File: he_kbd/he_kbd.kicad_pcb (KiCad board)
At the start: 2 copper layers, 162.2 x 126.5 mm, 175 parts

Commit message: more progress
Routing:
- net NEOPIXEL_POWER: track 914.5 -> 915.7 mm
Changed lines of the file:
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@@
 	)
 	(segment
-		(start 138.240183 50.844942)
+		(start 128.040183 50.844942)
 		(end 121.640183 50.844942)
 		(width 0.7)
@@
 	)
 	(segment
+		(start 138.240183 50.844942)
+		(end 128.040183 50.844942)
+		(width 0.7)
+		(layer "B.Cu")
+		(net 23)
+	)
+	(segment
 		(start 152.460183 85.544942)
 		(end 152.660183 85.344942)
@@
 	)
 	(segment
+		(start 127.990183 50.894942)
+		(end 128.040183 50.844942)
+		(width 0.7)
+		(layer "B.Cu")
+		(net 23)
+	)
+	(segment
 		(start 60.590183 129.094942)
 		(end 59.090183 129.094942)
@@
 		(width 0.7)
 		(layer "B.Cu")
+		(net 23)
+	)
+	(segment
+		(start 127.990183 52.044942)
+		(end 127.990183 50.894942)
+		(width 0.7)
+		(layer "B.Cu")

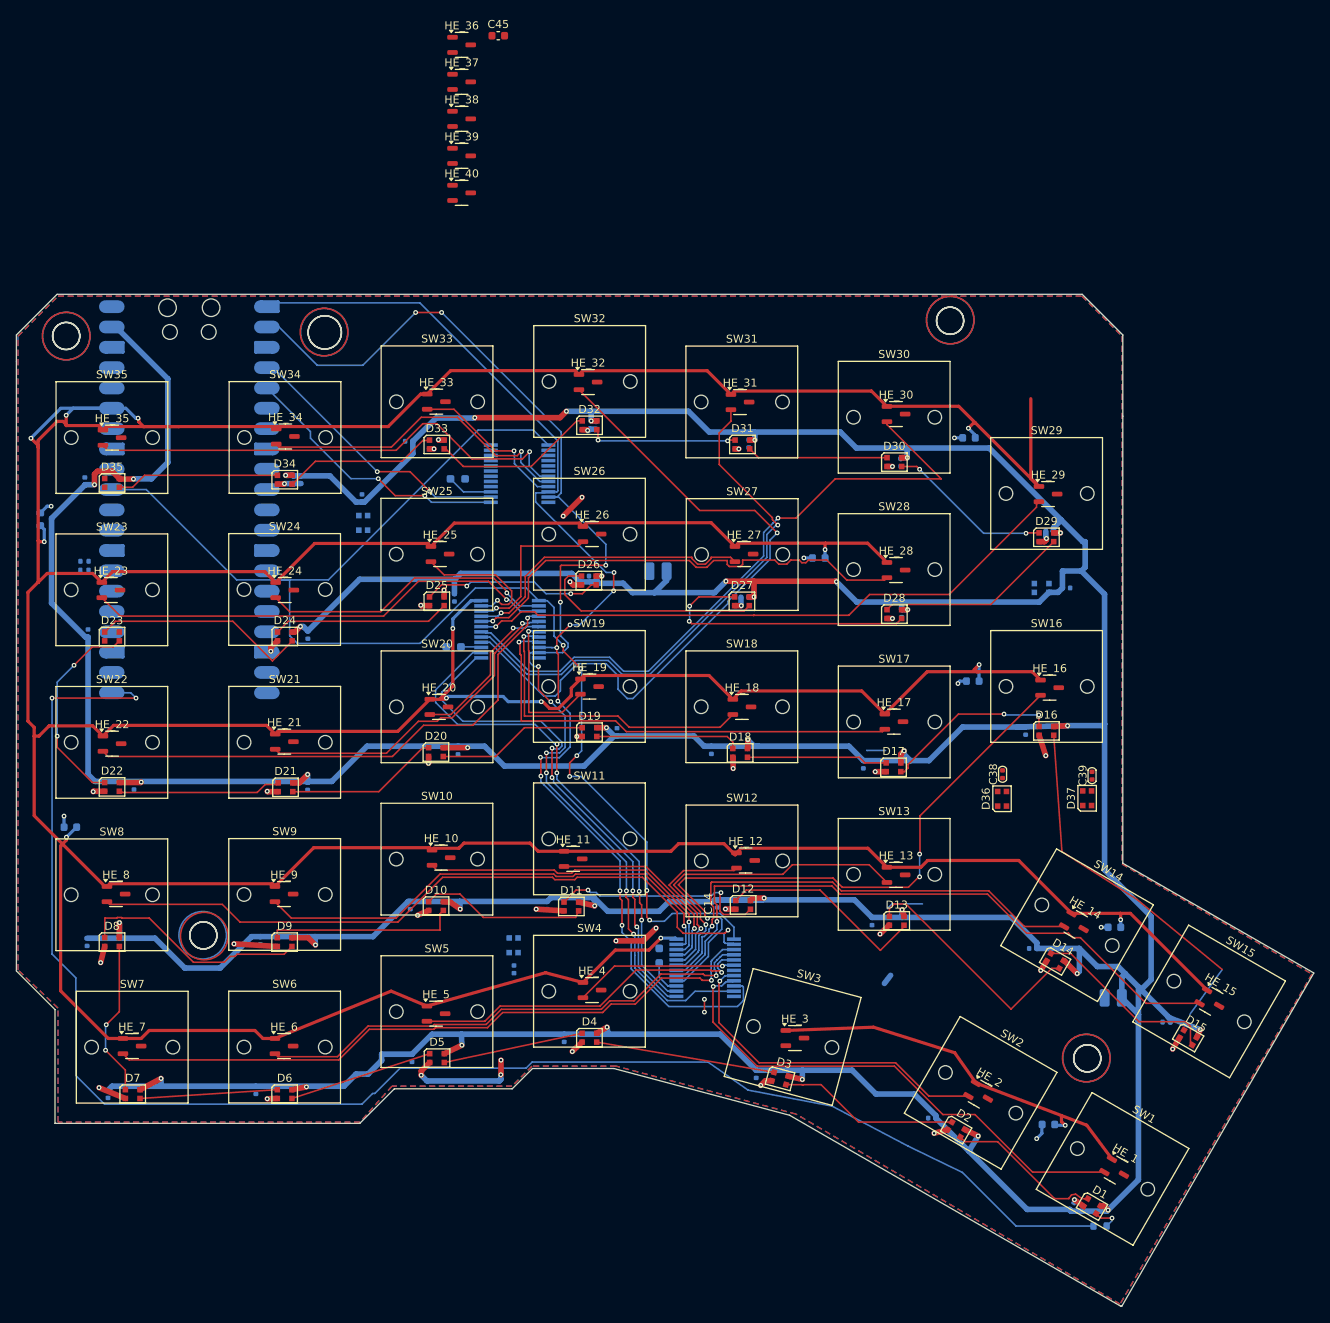
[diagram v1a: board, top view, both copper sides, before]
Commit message: realised have to change capacitor footprint entirely
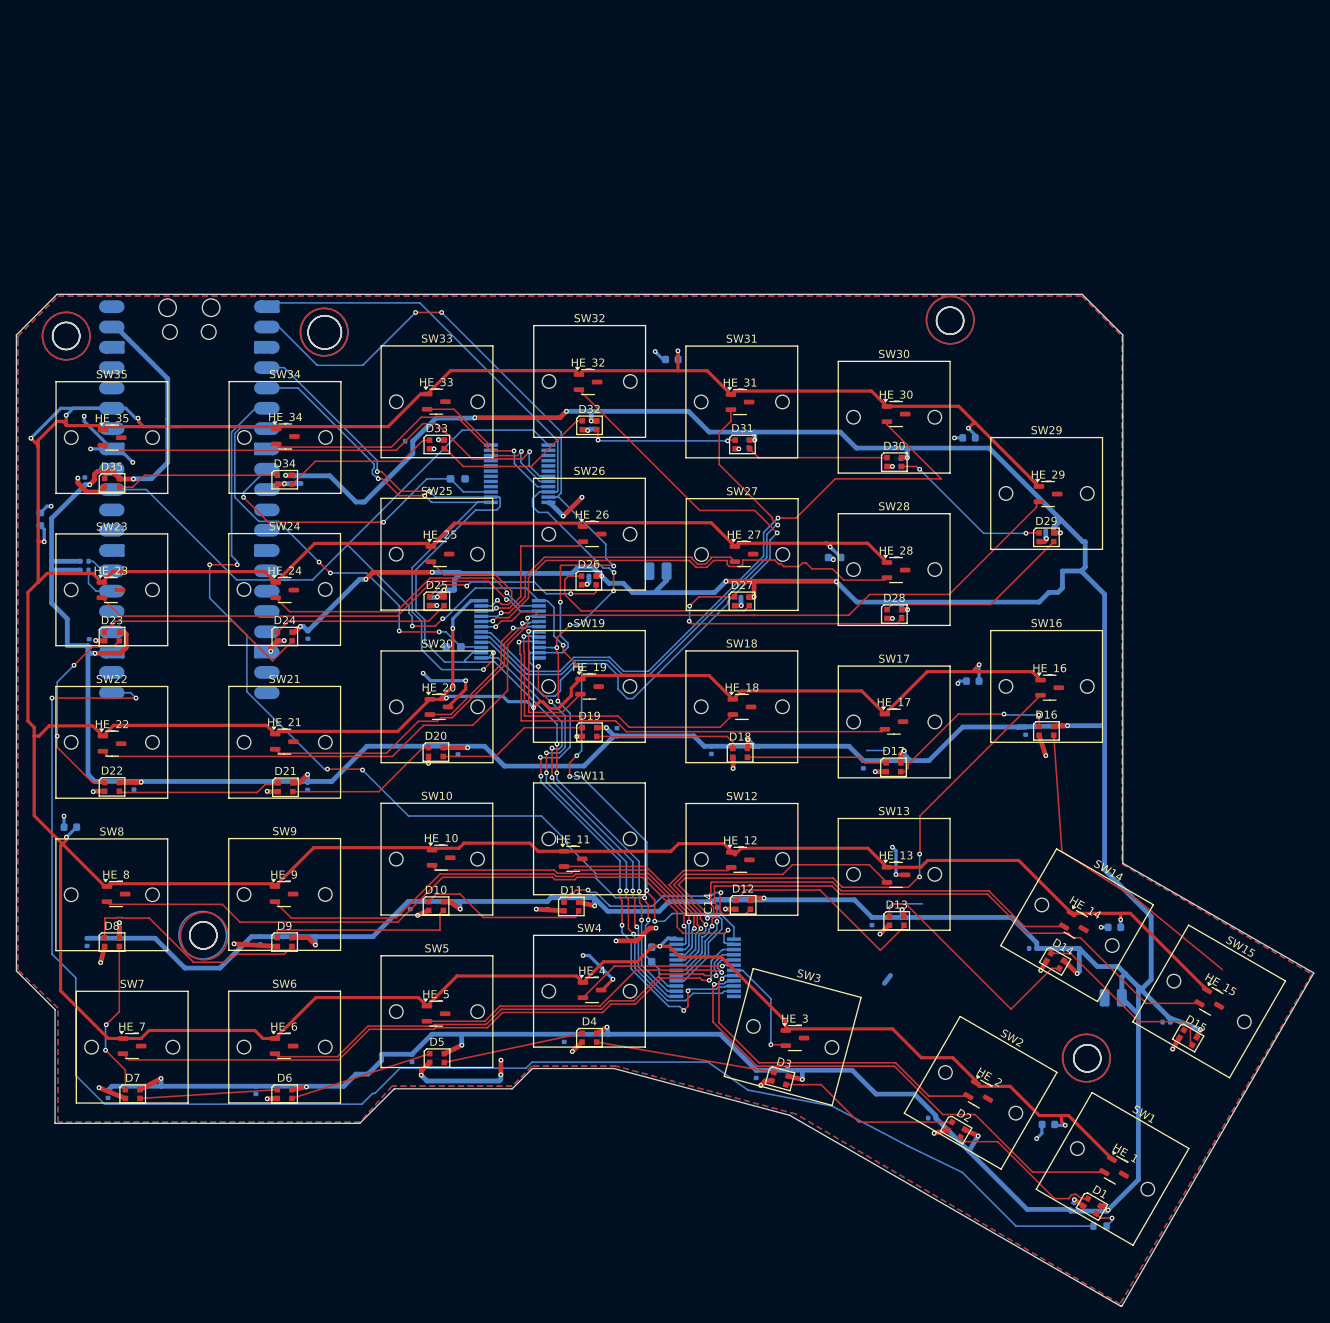
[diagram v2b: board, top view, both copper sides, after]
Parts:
- removed C38, C39, C40, C41, C42: 100n, PCM_Capacitor_SMD_AKL:C_0402_1005Metric
- removed D36, D37, D38, D39, D40: WS2812B-2020, LED_SMD:LED_WS2812B-2020_PLCC4_2.0x2.0mm
- removed HE_36, HE_37, HE_38, HE_39, HE_40: ~, Package_TO_SOT_SMD:SOT-23-3
- C45: moved to B.Cu
- moved C45 45.9 mm to (98.6, 39.8), turned to 180 degrees
- moved C27 3.02 mm to (68.4, 70.0)
- moved C47 1.98 mm to (118.9, 64.5)
- moved C25 1.24 mm to (25.7, 75.2)
- moved R9 0.95 mm to (96.1, 114.1)
- moved HE_12 0.66 mm to (107.1, 102.3)
- moved SW12 0.19 mm to (100.3, 95.2)
- turned R6 to 0 degrees
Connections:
- AM2 pad 2: /hesig40 -> unconnected-(AM2-I7-Pad2)
- AM2 pad 3: /hesig39 -> unconnected-(AM2-I6-Pad3)
- AM2 pad 4: /hesig38 -> unconnected-(AM2-I5-Pad4)
- AM2 pad 5: /hesig37 -> unconnected-(AM2-I4-Pad5)
- AM2 pad 6: /hesig36 -> unconnected-(AM2-I3-Pad6)
- D35 pad 1: Net-(D35-DOUT) -> unconnected-(D35-DOUT-Pad1)
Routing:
- net /MTP_EN_0: track 4.38 -> 118.3 mm, vias 0 -> 6
- net /MTP_EN_1: track 2.57 -> 52.7 mm, vias 0 -> 4
- net /ANALOGUE_GND: track 9.37 -> 44.2 mm, vias 7 -> 17
- net /MTP_EN_2: track 5.72 -> 39.8 mm, vias 0 -> 2
- net /MTP_BIN_3: track 99.3 -> 128.1 mm, vias 6 -> 8
- net /MTP_BIN_2: track 98.9 -> 124.8 mm
- net NEOPIXEL_POWER: track 915.7 -> 938.2 mm, vias 39 -> 43
- net /ANALOGUE_VIN: track 825.6 -> 845.5 mm, vias 14 -> 15
- net /hesig3: track 0.00 -> 13.8 mm, vias 0 -> 1
- net /AN_SIG: track 172.4 -> 162.0 mm, vias 6 -> 8
- net GND: track 82.0 -> 90.2 mm, vias 41 -> 42
- net Net-(D15-DOUT): track 46.4 -> 39.5 mm
- net I2C0_SDA: track 0.00 -> 4.98 mm
- net I2C0_SCL: track 0.00 -> 3.40 mm
- net /MTP_BIN_1: track 153.4 -> 155.0 mm
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
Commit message: i will have to change the led footprint as well lets go
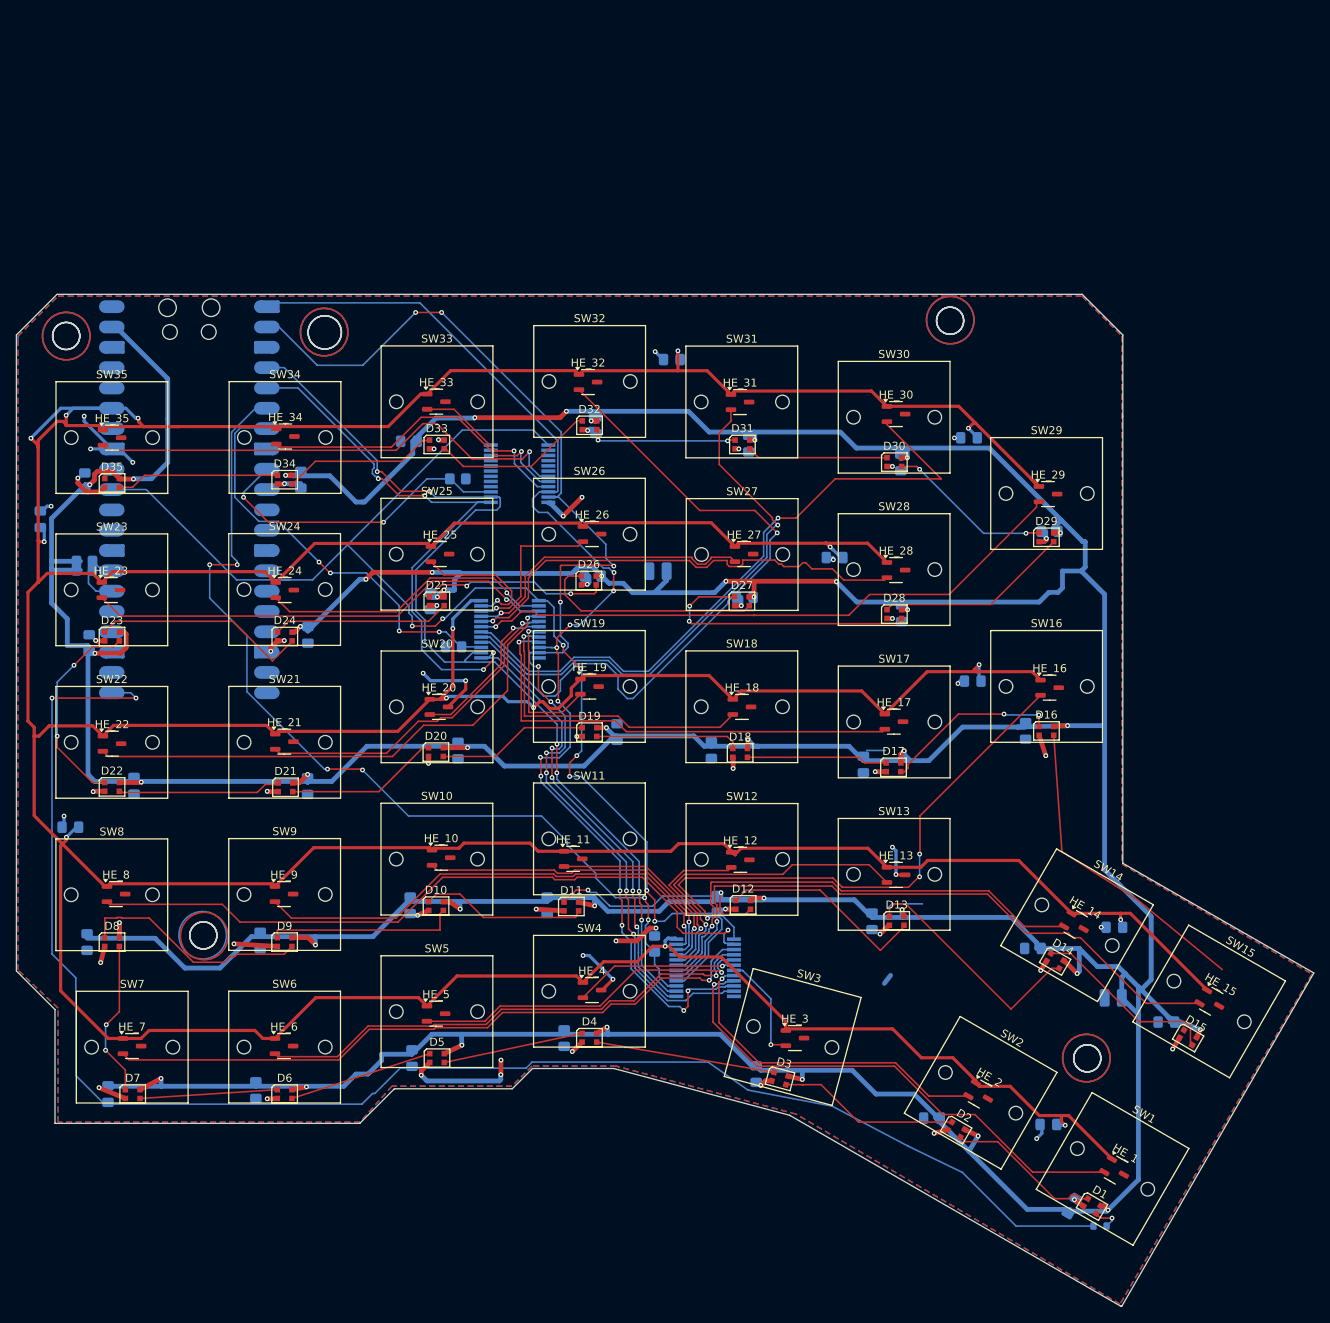
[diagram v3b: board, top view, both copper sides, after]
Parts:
- C10, C11, C12, C13, C14, C15, C16, C17, C18, C19, C20, C21, C22, C23, C24, C25, C26, C27, C28, C29, C3, C30, C31, C32, C33, C34, C35, C36, C37, C4, C5, C6, C7, C8, C9: footprint PCM_Capacitor_SMD_AKL:C_0402_1005Metric -> PCM_Capacitor_SMD_AKL:C_0805_2012Metric_Pad1.18x1.45mm_HandSolder
- C43, C44, C45, C46, C47, C48, C49, C50: footprint Inductor_SMD:L_0603_1608Metric -> PCM_Capacitor_SMD_AKL:C_0805_2012Metric_Pad1.18x1.45mm_HandSolder
- R5, R6: footprint Resistor_SMD:R_0402_1005Metric -> Resistor_SMD:R_0805_2012Metric_Pad1.20x1.40mm_HandSolder
- R7, R8, R9: footprint Resistor_SMD:R_0603_1608Metric_Pad0.98x0.95mm_HandSolder -> Resistor_SMD:R_0805_2012Metric_Pad1.20x1.40mm_HandSolder
- moved R9 1.36 mm to (96.4, 112.8)

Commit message: regaining progress, slowly remapping the broken connectiosn
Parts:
- D1, D10, D11, D12, D13, D14, D15, D16, D17, D18, D19, D2, D20, D21, D22, D23, D24, D25, D26, D27, D28, D29, D3, D30, D31, D32, D33, D34, D35, D4, D5, D6, D7, D8, D9: value WS2812B-2020 -> WS2812B; footprint LED_SMD:LED_WS2812B-2020_PLCC4_2.0x2.0mm -> LED_SMD:LED_WS2812B_PLCC4_5.0x5.0mm_P3.2mm
- moved C13 5.42 mm to (88.3, 106.9)
- moved C19 3.96 mm to (126.4, 90.9)
- moved C20 3.80 mm to (107.2, 89.3)
- moved C8 3.65 mm to (50.2, 131.7)
- moved C17 3.60 mm to (162.8, 125.3), turned to -90 degrees
- moved C4 3.56 mm to (133.9, 136.8), turned to -120 degrees
- moved C12 3.41 mm to (69.3, 108.4)
- moved C21 3.28 mm to (88.4, 86.6), turned to -90 degrees
- moved HE_11 3.18 mm to (88.2, 99.7)
- moved C9 3.15 mm to (31.2, 132.0)
- moved C7 3.00 mm to (69.1, 127.2)
- moved C11 2.99 mm to (50.1, 112.6)
- moved D11 2.99 mm to (88.3, 106.3)
- moved C10 2.97 mm to (28.4, 112.7)
- moved C16 2.89 mm to (146.1, 115.0), turned to -90 degrees
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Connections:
- D1 pad 1: Net-(D1-DOUT) -> NEOPIXEL_POWER
- D1 pad 2: GND -> Net-(D1-DOUT)
- D1 pad 3: Net-(D1-DIN) -> GND
- D1 pad 4: NEOPIXEL_POWER -> Net-(D1-DIN)
- D10 pad 1: Net-(D10-DOUT) -> NEOPIXEL_POWER
- D10 pad 2: GND -> Net-(D10-DOUT)
- D10 pad 3: Net-(D10-DIN) -> GND
- D10 pad 4: NEOPIXEL_POWER -> Net-(D10-DIN)
- D11 pad 1: Net-(D11-DOUT) -> NEOPIXEL_POWER
- D11 pad 2: GND -> Net-(D11-DOUT)
- D11 pad 3: Net-(D10-DOUT) -> GND
- D11 pad 4: NEOPIXEL_POWER -> Net-(D10-DOUT)
- D12 pad 1: Net-(D12-DOUT) -> NEOPIXEL_POWER
- D12 pad 2: GND -> Net-(D12-DOUT)
- D12 pad 3: Net-(D11-DOUT) -> GND
- D12 pad 4: NEOPIXEL_POWER -> Net-(D11-DOUT)
- D13 pad 1: Net-(D13-DOUT) -> NEOPIXEL_POWER
- D13 pad 2: GND -> Net-(D13-DOUT)
- D13 pad 3: Net-(D12-DOUT) -> GND
- D13 pad 4: NEOPIXEL_POWER -> Net-(D12-DOUT)
- D14 pad 1: Net-(D14-DOUT) -> NEOPIXEL_POWER
- D14 pad 2: GND -> Net-(D14-DOUT)
- D14 pad 3: Net-(D13-DOUT) -> GND
- D14 pad 4: NEOPIXEL_POWER -> Net-(D13-DOUT)
- D15 pad 1: Net-(D15-DOUT) -> NEOPIXEL_POWER
- D15 pad 2: GND -> Net-(D15-DOUT)
- D15 pad 3: Net-(D14-DOUT) -> GND
- D15 pad 4: NEOPIXEL_POWER -> Net-(D14-DOUT)
- D16 pad 1: Net-(D16-DOUT) -> NEOPIXEL_POWER
- D16 pad 2: GND -> Net-(D16-DOUT)
- D16 pad 3: Net-(D15-DOUT) -> GND
- D16 pad 4: NEOPIXEL_POWER -> Net-(D15-DOUT)
- D17 pad 1: Net-(D17-DOUT) -> NEOPIXEL_POWER
- D17 pad 2: GND -> Net-(D17-DOUT)
- D17 pad 3: Net-(D16-DOUT) -> GND
- D17 pad 4: NEOPIXEL_POWER -> Net-(D16-DOUT)
- D18 pad 1: Net-(D18-DOUT) -> NEOPIXEL_POWER
- D18 pad 2: GND -> Net-(D18-DOUT)
- D18 pad 3: Net-(D17-DOUT) -> GND
- D18 pad 4: NEOPIXEL_POWER -> Net-(D17-DOUT)
- D19 pad 1: Net-(D19-DOUT) -> NEOPIXEL_POWER
- D19 pad 2: GND -> Net-(D19-DOUT)
- D19 pad 3: Net-(D18-DOUT) -> GND
- D19 pad 4: NEOPIXEL_POWER -> Net-(D18-DOUT)
- D2 pad 1: Net-(D2-DOUT) -> NEOPIXEL_POWER
- D2 pad 2: GND -> Net-(D2-DOUT)
- D2 pad 3: Net-(D1-DOUT) -> GND
- D2 pad 4: NEOPIXEL_POWER -> Net-(D1-DOUT)
- D20 pad 1: Net-(D20-DOUT) -> NEOPIXEL_POWER
- D20 pad 2: GND -> Net-(D20-DOUT)
- D20 pad 3: Net-(D19-DOUT) -> GND
- D20 pad 4: NEOPIXEL_POWER -> Net-(D19-DOUT)
- D21 pad 1: Net-(D21-DOUT) -> NEOPIXEL_POWER
- D21 pad 2: GND -> Net-(D21-DOUT)
- D21 pad 3: Net-(D20-DOUT) -> GND
- D21 pad 4: NEOPIXEL_POWER -> Net-(D20-DOUT)
- D22 pad 1: Net-(D22-DOUT) -> NEOPIXEL_POWER
- D22 pad 2: GND -> Net-(D22-DOUT)
- D22 pad 3: Net-(D21-DOUT) -> GND
- D22 pad 4: NEOPIXEL_POWER -> Net-(D21-DOUT)
- D23 pad 1: Net-(D23-DOUT) -> NEOPIXEL_POWER
- D23 pad 2: GND -> Net-(D23-DOUT)
- D23 pad 3: Net-(D22-DOUT) -> GND
- D23 pad 4: NEOPIXEL_POWER -> Net-(D22-DOUT)
- D24 pad 1: Net-(D24-DOUT) -> NEOPIXEL_POWER
- D24 pad 2: GND -> Net-(D24-DOUT)
- D24 pad 3: Net-(D23-DOUT) -> GND
- D24 pad 4: NEOPIXEL_POWER -> Net-(D23-DOUT)
- D25 pad 1: Net-(D25-DOUT) -> NEOPIXEL_POWER
- D25 pad 2: GND -> Net-(D25-DOUT)
- D25 pad 3: Net-(D24-DOUT) -> GND
- D25 pad 4: NEOPIXEL_POWER -> Net-(D24-DOUT)
- D26 pad 1: Net-(D26-DOUT) -> NEOPIXEL_POWER
- D26 pad 2: GND -> Net-(D26-DOUT)
- D26 pad 3: Net-(D25-DOUT) -> GND
- D26 pad 4: NEOPIXEL_POWER -> Net-(D25-DOUT)
- D27 pad 1: Net-(D27-DOUT) -> NEOPIXEL_POWER
- D27 pad 2: GND -> Net-(D27-DOUT)
- D27 pad 3: Net-(D26-DOUT) -> GND
- D27 pad 4: NEOPIXEL_POWER -> Net-(D26-DOUT)
- D28 pad 1: Net-(D28-DOUT) -> NEOPIXEL_POWER
- D28 pad 2: GND -> Net-(D28-DOUT)
- D28 pad 3: Net-(D27-DOUT) -> GND
- D28 pad 4: NEOPIXEL_POWER -> Net-(D27-DOUT)
- D29 pad 1: Net-(D29-DOUT) -> NEOPIXEL_POWER
- D29 pad 2: GND -> Net-(D29-DOUT)
- D29 pad 3: Net-(D28-DOUT) -> GND
- D29 pad 4: NEOPIXEL_POWER -> Net-(D28-DOUT)
- D3 pad 1: Net-(D3-DOUT) -> NEOPIXEL_POWER
- D3 pad 2: GND -> Net-(D3-DOUT)
- D3 pad 3: Net-(D2-DOUT) -> GND
- D3 pad 4: NEOPIXEL_POWER -> Net-(D2-DOUT)
- D30 pad 1: Net-(D30-DOUT) -> NEOPIXEL_POWER
- D30 pad 2: GND -> Net-(D30-DOUT)
- D30 pad 3: Net-(D29-DOUT) -> GND
- D30 pad 4: NEOPIXEL_POWER -> Net-(D29-DOUT)
- D31 pad 1: Net-(D31-DOUT) -> NEOPIXEL_POWER
- D31 pad 2: GND -> Net-(D31-DOUT)
- D31 pad 3: Net-(D30-DOUT) -> GND
- D31 pad 4: NEOPIXEL_POWER -> Net-(D30-DOUT)
- D32 pad 1: Net-(D32-DOUT) -> NEOPIXEL_POWER
- D32 pad 2: GND -> Net-(D32-DOUT)
- D32 pad 3: Net-(D31-DOUT) -> GND
- D32 pad 4: NEOPIXEL_POWER -> Net-(D31-DOUT)
- D33 pad 1: Net-(D33-DOUT) -> NEOPIXEL_POWER
- D33 pad 2: GND -> Net-(D33-DOUT)
- D33 pad 3: Net-(D32-DOUT) -> GND
- D33 pad 4: NEOPIXEL_POWER -> Net-(D32-DOUT)
- D34 pad 1: Net-(D34-DOUT) -> NEOPIXEL_POWER
- D34 pad 2: GND -> Net-(D34-DOUT)
- D34 pad 3: Net-(D33-DOUT) -> GND
- D34 pad 4: NEOPIXEL_POWER -> Net-(D33-DOUT)
- D35 pad 1: unconnected-(D35-DOUT-Pad1) -> NEOPIXEL_POWER
- D35 pad 2: GND -> unconnected-(D35-DOUT-Pad2)
- D35 pad 3: Net-(D34-DOUT) -> GND
- D35 pad 4: NEOPIXEL_POWER -> Net-(D34-DOUT)
- D4 pad 1: Net-(D4-DOUT) -> NEOPIXEL_POWER
- D4 pad 2: GND -> Net-(D4-DOUT)
- D4 pad 3: Net-(D3-DOUT) -> GND
- D4 pad 4: NEOPIXEL_POWER -> Net-(D3-DOUT)
- D5 pad 1: Net-(D5-DOUT) -> NEOPIXEL_POWER
- D5 pad 2: GND -> Net-(D5-DOUT)
- D5 pad 3: Net-(D4-DOUT) -> GND
- D5 pad 4: NEOPIXEL_POWER -> Net-(D4-DOUT)
- D6 pad 1: Net-(D6-DOUT) -> NEOPIXEL_POWER
- D6 pad 2: GND -> Net-(D6-DOUT)
- D6 pad 3: Net-(D5-DOUT) -> GND
- D6 pad 4: NEOPIXEL_POWER -> Net-(D5-DOUT)
- D7 pad 1: Net-(D7-DOUT) -> NEOPIXEL_POWER
- D7 pad 2: GND -> Net-(D7-DOUT)
- D7 pad 3: Net-(D6-DOUT) -> GND
- D7 pad 4: NEOPIXEL_POWER -> Net-(D6-DOUT)
- D8 pad 1: Net-(D8-DOUT) -> NEOPIXEL_POWER
- D8 pad 2: GND -> Net-(D8-DOUT)
- D8 pad 3: Net-(D7-DOUT) -> GND
- D8 pad 4: NEOPIXEL_POWER -> Net-(D7-DOUT)
- D9 pad 1: Net-(D10-DIN) -> NEOPIXEL_POWER
- D9 pad 2: GND -> Net-(D10-DIN)
- D9 pad 3: Net-(D8-DOUT) -> GND
- D9 pad 4: NEOPIXEL_POWER -> Net-(D8-DOUT)
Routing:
- net /hesig35: track 61.9 -> 0.00 mm, vias 1 -> 0
- net /AN_SIG: track 162.0 -> 101.4 mm, vias 8 -> 2
- net /hesig34: track 40.4 -> 0.00 mm, vias 1 -> 0
- net Net-(D27-DOUT): track 35.0 -> 0.00 mm, vias 2 -> 0
- net GND: track 90.2 -> 124.7 mm, vias 42 -> 35
- net /MTP_BIN_1: track 155.0 -> 122.7 mm, vias 10 -> 8
- net /MTP_BIN_0: track 149.5 -> 119.4 mm, vias 11 -> 8
- net Net-(D26-DOUT): track 28.3 -> 0.00 mm
- net Net-(D23-DOUT): track 27.1 -> 0.00 mm
- net Net-(D22-DOUT): track 25.9 -> 0.00 mm, vias 2 -> 0
- net Net-(D28-DOUT): track 24.4 -> 0.00 mm
- net Net-(D25-DOUT): track 23.3 -> 0.00 mm, vias 2 -> 0
- net Net-(D24-DOUT): track 22.2 -> 0.00 mm
- net Net-(D29-DOUT): track 20.7 -> 0.00 mm, vias 2 -> 0
- net Net-(D32-DOUT): track 20.5 -> 0.00 mm
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
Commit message: almost done
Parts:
- moved C35 3.35 mm to (68.9, 50.9), turned to -90 degrees
- moved C34 1.10 mm to (88.2, 48.6)
- moved D34 0.82 mm to (50.1, 55.6)
- moved D33 0.74 mm to (69.2, 51.1)
- moved D32 0.71 mm to (88.2, 48.7)
- moved C36 0.62 mm to (52.2, 55.4)
- moved D35 0.44 mm to (28.5, 55.6)
- turned C37 to -90 degrees
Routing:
- net /AN_SIG: track 101.4 -> 265.8 mm, vias 2 -> 12
- net /hesig35: track 0.00 -> 59.2 mm, vias 0 -> 1
- net /MTP_BIN_1: track 122.7 -> 168.9 mm, vias 8 -> 12
- net /hesig34: track 0.00 -> 40.2 mm, vias 0 -> 1
- net /MTP_BIN_0: track 119.4 -> 158.0 mm, vias 8 -> 11
- net Net-(D25-DOUT): track 0.00 -> 30.9 mm, vias 0 -> 2
- net Net-(D23-DOUT): track 0.00 -> 30.0 mm, vias 0 -> 2
- net Net-(D28-DOUT): track 0.00 -> 29.6 mm
- net Net-(D22-DOUT): track 0.00 -> 29.0 mm, vias 0 -> 2
- net NEOPIXEL_POWER: track 935.6 -> 962.7 mm, vias 39 -> 43
- net Net-(D24-DOUT): track 0.00 -> 27.1 mm
- net Net-(D27-DOUT): track 0.00 -> 25.8 mm
- net Net-(D26-DOUT): track 0.00 -> 25.4 mm, vias 0 -> 2
- net Net-(D29-DOUT): track 0.00 -> 19.5 mm
- net Net-(D21-DOUT): track 0.00 -> 18.2 mm
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
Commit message: I think it may be done... lets see how broken it is
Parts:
- added J2: Conn_01x08_Pin, Connector_PinHeader_1.27mm:PinHeader_1x08_P1.27mm_Horizontal, B.Cu at (93.1, 51.4)
- moved R6 1.66 mm to (23.6, 64.3)
- moved R5 1.53 mm to (23.6, 66.4)
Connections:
- AM2 pad 2: unconnected-(AM2-I7-Pad2) -> Net-(AM2-I7)
- AM2 pad 21: unconnected-(AM2-I10-Pad21) -> Net-(AM2-I10)
- AM2 pad 22: unconnected-(AM2-I9-Pad22) -> Net-(AM2-I9)
- AM2 pad 23: unconnected-(AM2-I8-Pad23) -> Net-(AM2-I8)
- AM2 pad 3: unconnected-(AM2-I6-Pad3) -> Net-(AM2-I6)
- AM2 pad 4: unconnected-(AM2-I5-Pad4) -> Net-(AM2-I5)
- AM2 pad 5: unconnected-(AM2-I4-Pad5) -> Net-(AM2-I4)
- AM2 pad 6: unconnected-(AM2-I3-Pad6) -> Net-(AM2-I3)
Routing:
- net /ANALOGUE_GND: track 55.2 -> 278.2 mm, vias 20 -> 44
- net GND: track 128.6 -> 242.4 mm, vias 40 -> 53
- net /ANALOGUE_VIN: track 849.0 -> 930.0 mm, vias 17 -> 18
- net Net-(AM2-I8): track 0.00 -> 50.0 mm
- net Net-(AM2-I7): track 0.00 -> 39.2 mm, vias 0 -> 1
- net Net-(AM2-I6): track 0.00 -> 32.6 mm, vias 0 -> 1
- net Net-(AM2-I5): track 0.00 -> 31.9 mm, vias 0 -> 1
- net Net-(AM2-I4): track 0.00 -> 30.7 mm, vias 0 -> 1
- net Net-(AM2-I3): track 0.00 -> 29.4 mm
- net Net-(AM2-I10): track 0.00 -> 24.9 mm, vias 0 -> 1
- net Net-(AM2-I9): track 0.00 -> 22.3 mm, vias 0 -> 1
- net NEOPIXEL_POWER: track 962.7 -> 977.2 mm
- net /MTP_EN_0: track 121.4 -> 126.2 mm
- net I2C0_SCL: track 0.00 -> 4.71 mm
- net /hesig34: track 40.2 -> 43.3 mm
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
